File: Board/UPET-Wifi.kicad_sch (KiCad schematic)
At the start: 11 parts, among them U1 ESP32-C3-WROOM-02, U2 SC16IS752IPW, U3 1.8432 MHz

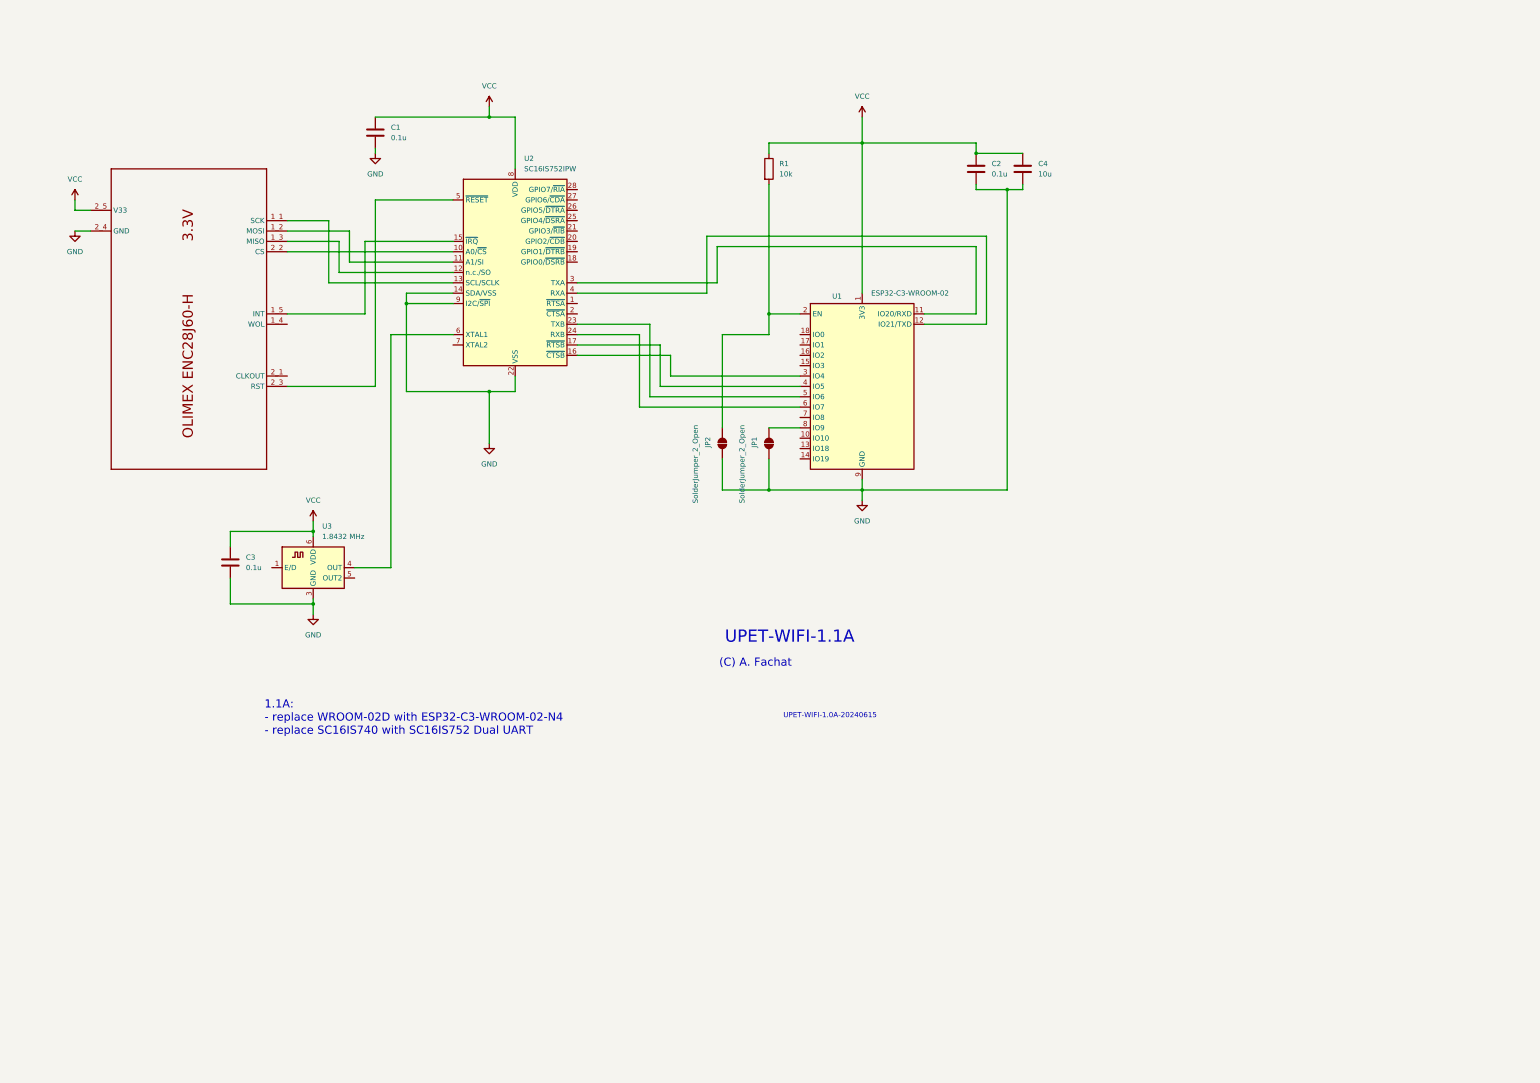
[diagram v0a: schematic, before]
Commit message: move to 1.2 - separate serial prog interface
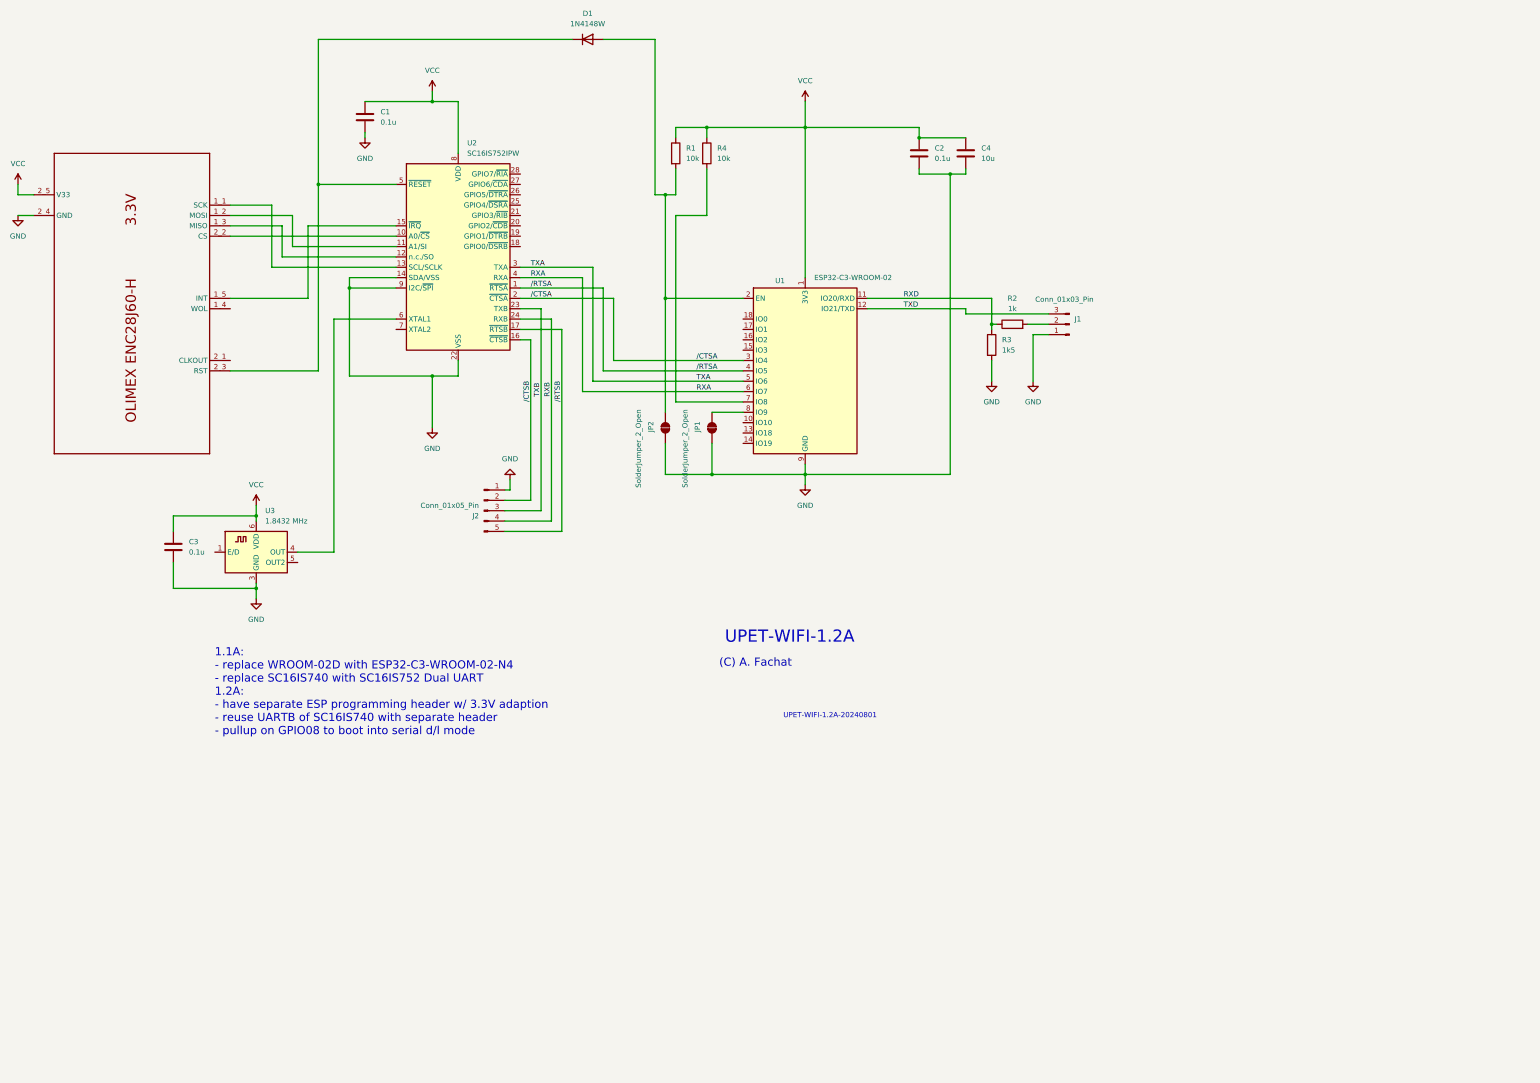
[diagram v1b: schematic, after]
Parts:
- added D1: 1N4148W, Diode_SMD:D_SOD-123, symbol Diode:1N4148W
- added J1: Conn_01x03_Pin, Connector_PinHeader_2.54mm:PinHeader_1x03_P2.54mm_Vertical, symbol Connector:Conn_01x03_Pin
- added J2: Conn_01x05_Pin, Connector_PinHeader_2.54mm:PinHeader_1x05_P2.54mm_Vertical, symbol Connector:Conn_01x05_Pin
- added R2: 1k, Resistor_SMD:R_0603_1608Metric_Pad0.98x0.95mm_HandSolder, symbol Device:R
- added R3: 1k5, Resistor_SMD:R_0603_1608Metric_Pad0.98x0.95mm_HandSolder, symbol Device:R
- added R4: 10k, Resistor_SMD:R_0603_1608Metric_Pad0.98x0.95mm_HandSolder, symbol Device:R
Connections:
- net GND: now also J1.1 (Pin_1), J2.1 (Pin_1), R3.2
- net VCC: now also R4.1
- net at U$1.2_3 (RST), U2.5 (~{RESET}): now also D1.1 (K)
- net at JP2.2 (B), R1.2, U1.2 (EN): now also D1.2 (A)
- net RXD: now reaches U1.11 (IO20/RXD)
- net RXD: now also R2.1, R3.1; no longer U2.3 (TXA)
- net RXA: now reaches U2.4 (RXA)
- net RXA: now also U1.6 (IO7); no longer U1.12 (IO21/TXD)
- net /CTSA: now reaches U1.3 (IO4)
- net /CTSA: now also U2.2 (~{CTSA}); no longer U2.16 (~{CTSB})
- net /RTSA: now reaches U1.4 (IO5)
- net /RTSA: now also U2.1 (~{RTSA}); no longer U2.17 (~{RTSB})
- net TXA: now reaches U1.5 (IO6)
- net TXA: now also U2.3 (TXA); no longer U2.23 (TXB)
- net RXB: now reaches U2.24 (RXB)
- net RXB: now also J2.4 (Pin_4); no longer U1.6 (IO7)
- net at U1.7 (IO8): now also R4.2
- new net: J1.2 (Pin_2), R2.2
- new net TXB: J2.3 (Pin_3), U2.23 (TXB)
- new net TXD: J1.3 (Pin_3), U1.12 (IO21/TXD)
- new net /CTSB: J2.2 (Pin_2), U2.16 (~{CTSB})
- new net /RTSB: J2.5 (Pin_5), U2.17 (~{RTSB})
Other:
- note added: "1.1A: - replace WROOM-02D with ESP32-C3-WROOM-02-N4 - replace SC16IS740 with SC16IS752 Dual UART 1.2A: - have separate ESP programming header w/ 3.3V adaption - reuse UARTB of SC16IS740 with separate header - pullup on GPIO08 to boot into serial d/l mode"
- note added: "UPET-WIFI-1.2A"
- note added: "UPET-WIFI-1.2A-20240801"
- note removed: "1.1A: - replace WROOM-02D with ESP32-C3-WROOM-02-N4 - replace SC16IS740 with SC16IS752 Dual UART"
- note removed: "UPET-WIFI-1.0A-20240615"
- note removed: "UPET-WIFI-1.1A"
- moved on the sheet: C1, C2, C3, C4, JP1, JP2, R1, U1, U2, U3

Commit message: work on wifi 1.3a
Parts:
- removed J1: Conn_01x03_Pin, Connector_PinHeader_2.54mm:PinHeader_1x03_P2.54mm_Vertical, symbol Connector:Conn_01x03_Pin
- removed J2: Conn_01x05_Pin, Connector_PinHeader_2.54mm:PinHeader_1x05_P2.54mm_Vertical, symbol Connector:Conn_01x05_Pin
- added J1: Conn_01x06, Connector_PinHeader_2.54mm:PinHeader_1x06_P2.54mm_Vertical, symbol Connector_Generic:Conn_01x06
- added J3: Conn_01x09, Connector_PinHeader_2.54mm:PinHeader_1x09_P2.54mm_Vertical, symbol Connector_Generic:Conn_01x09
- added Q1, Q2: S8050, Package_TO_SOT_SMD:SOT-23, symbol Transistor_BJT:S8050
- added R5, R6: 12k, Resistor_SMD:R_0603_1608Metric_Pad0.98x0.95mm_HandSolder, symbol Device:R
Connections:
- net GND: now also J1.1 (Pin_1), J3.1 (Pin_1)
- net RXB: now also J3.4 (Pin_4)
- net TXB: now also J3.3 (Pin_3)
- net TXD: now also J1.4 (Pin_4)
- net /CTSB: now also J3.2 (Pin_2)
- net /RTSB: now also J3.5 (Pin_5)
- net at D1.2 (A), JP2.2 (B), R1.2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: now also Q1.3 (C)
- net at JP1.2 (B), U1.8 (IO9): now also Q2.3 (C)
- net at R2.2: now also J1.3 (Pin_3)
- net /DSRB: now reaches U2.18 (GPIO0/~{DSRB})
- net /DSRB: now also J3.6 (Pin_6)
- net /DTRB: now reaches U2.19 (GPIO1/~{DTRB})
- net /DTRB: now also J3.7 (Pin_7)
- net /CDB: now reaches U2.20 (GPIO2/~{CDB})
- net /CDB: now also J3.8 (Pin_8)
- net /RIB: now reaches U2.21 (GPIO3/~{RIB})
- net /RIB: now also J3.9 (Pin_9)
- new net: Q2.1 (B), R5.1
- new net: J1.6 (Pin_6), Q2.2 (E), R6.2
- new net: J1.2 (Pin_2), Q1.2 (E), R5.2
- new net: Q1.1 (B), R6.1
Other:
- moved on the sheet: R2, R3

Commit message: production files
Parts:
- added JP3: SolderJumper_2_Open, Jumper:SolderJumper-2_P1.3mm_Open_RoundedPad1.0x1.5mm, symbol Jumper:SolderJumper_2_Open
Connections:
- net RXD: now also JP3.2 (B)
- net at J1.3 (Pin_3), R2.2: now also JP3.1 (A)
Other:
- note added: "1.1A: - replace WROOM-02D with ESP32-C3-WROOM-02-N4 - replace SC16IS740 with SC16IS752 Dual UART 1.2A: - have separate ESP programming header w/ 3.3V adaption - reuse UARTB of SC16IS740 with separate header - pullup on GPIO08 to boot into serial d/l mode 1.3A: - wider serial connectors - allow use of /RTS and /DTR for ESP control - Programming serial option 3.3V/5V via JP3"
- note added: "Short JP3 if Programming with 3.3V"
- note added: "UPET-WIFI-1.3A"
- note added: "UPET-WIFI-1.3A-20250122"
- note removed: "1.1A: - replace WROOM-02D with ESP32-C3-WROOM-02-N4 - replace SC16IS740 with SC16IS752 Dual UART 1.2A: - have separate ESP programming header w/ 3.3V adaption - reuse UARTB of SC16IS740 with separate header - pullup on GPIO08 to boot into serial d/l mode"
- note removed: "UPET-WIFI-1.2A"
- note removed: "UPET-WIFI-1.2A-20240801"
- moved on the sheet: C3, U3
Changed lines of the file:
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@@
 	(paper "A4")
 	(junction
-		(at 76.2 158.75)
+		(at 86.36 148.59)
 		(diameter 0)
 		(color 0 0 0 0)
@@
 	)
 	(junction
+		(at 255.27 87.63)
+		(diameter 0)
+		(color 0 0 0 0)
+	)
+	(junction
 		(at 190.5 115.57)
 		(diameter 0)
@@
 	)
 	(junction
-		(at 76.2 140.97)
+		(at 86.36 130.81)
 		(diameter 0)
 		(color 0 0 0 0)
@@
 	(wire
 		(pts
-			(xy 86.36 149.86) (xy 95.25 149.86)
+			(xy 96.52 139.7) (xy 105.41 139.7)
 		)
 		(stroke
@@
 	(wire
 		(pts
+			(xy 255.27 77.47) (xy 255.27 87.63)
+		)
+		(stroke
+			(width 0)
+			(type default)
+		)
+	)
+	(wire
+		(pts
 			(xy 210.82 130.81) (xy 187.96 130.81)
 		)
@@
 	(wire
 		(pts
-			(xy 76.2 138.43) (xy 76.2 140.97)
+			(xy 86.36 128.27) (xy 86.36 130.81)
 		)
 		(stroke
@@
 	(wire
 		(pts
+			(xy 255.27 87.63) (xy 271.78 87.63)
+		)
+		(stroke
+			(width 0)
+			(type default)
+		)
+	)
+	(wire
+		(pts
 			(xy 140.97 87.63) (xy 172.72 87.63)
 		)
@@
 	(wire
 		(pts
-			(xy 76.2 140.97) (xy 55.88 140.97)
+			(xy 86.36 130.81) (xy 66.04 130.81)
 		)
 		(stroke
@@
 	(wire
 		(pts
-			(xy 55.88 140.97) (xy 55.88 144.78)
+			(xy 66.04 130.81) (xy 66.04 134.62)
 		)
 		(stroke
@@
 	(wire
 		(pts
+			(xy 242.57 77.47) (xy 241.3 77.47)
+		)
+		(stroke
+			(width 0)
+			(type default)
+		)
+	)
+	(wire
+		(pts
 			(xy 88.9 69.85) (xy 88.9 87.63)
 		)
@@
 	(wire
 		(pts
-			(xy 76.2 157.48) (xy 76.2 158.75)
+			(xy 86.36 147.32) (xy 86.36 148.59)
 		)
 		(stroke
@@
 	(wire
 		(pts
-			(xy 55.88 158.75) (xy 55.88 152.4)
+			(xy 66.04 148.59) (xy 66.04 142.24)
 		)
 		(stroke
@@
 	(wire
 		(pts
-			(xy 95.25 92.71) (xy 110.49 92.71)
+			(xy 105.41 92.71) (xy 110.49 92.71)
 		)
 		(stroke
@@
 	(wire
 		(pts
-			(xy 76.2 158.75) (xy 76.2 161.29)
+			(xy 86.36 148.59) (xy 86.36 151.13)
 		)
 		(stroke
@@
 	(wire
 		(pts
-			(xy 76.2 140.97) (xy 76.2 142.24)
+			(xy 250.19 77.47) (xy 255.27 77.47)
+		)
+		(stroke
+			(width 0)
+			(type default)
+		)
+	)
+	(wire
+		(pts
+			(xy 86.36 130.81) (xy 86.36 132.08)
 		)
 		(stroke
@@
 	(wire
 		(pts
+			(xy 241.3 77.47) (xy 241.3 87.63)
+		)
+		(stroke
+			(width 0)
+			(type default)
+		)
+	)
+	(wire
+		(pts
 			(xy 238.76 48.26) (xy 238.76 45.72)
 		)
@@
 	(wire
 		(pts
-			(xy 95.25 149.86) (xy 95.25 92.71)
+			(xy 105.41 139.7) (xy 105.41 92.71)
 		)
 		(stroke
@@
 	(wire
 		(pts
-			(xy 250.19 87.63) (xy 271.78 87.63)
+			(xy 250.19 87.63) (xy 255.27 87.63)
 		)
 		(stroke
@@
 	(wire
 		(pts
-			(xy 76.2 158.75) (xy 55.88 158.75)
+			(xy 86.36 148.59) (xy 66.04 148.59)
 		)
 		(stroke
@@
 		)
 	)
-	(text "1.1A:\n- replace WROOM-02D with ESP32-C3-WROOM-02-N4\n- replace SC16IS740 with SC16IS752 Dual UART\n1.2A:\n- have separate ESP programming header w/ 3.3V adaption\n- reuse UARTB of SC16IS740 with separate header\n- pullup on GPIO08 to boot into serial d/l mode"
+	(text "1.1A:\n- replace WROOM-02D with ESP32-C3-WROOM-02-N4\n- replace SC16IS740 with SC16IS752 Dual UART\n1.2A:\n- have separate ESP programming header w/ 3.3V adaption\n- reuse UARTB of SC16IS740 with separate header\n- pullup on GPIO08 to boot into serial d/l mode\n1.3A:\n- wider serial connectors\n- allow use of /RTS and /DTR for ESP control\n- Programming serial option 3.3V/5V via JP3"
 		(exclude_from_sim no)
-		(at 66.04 184.15 0)
+		(at 38.862 177.8 0)
 		(effects
 			(font
@@
 		)
 	)
-	(text "UPET-WIFI-1.2A\n"
+	(text "Short JP3 if\nProgramming\nwith 3.3V"
+		(exclude_from_sim no)
+		(at 253.492 73.152 0)
+		(effects
+			(font
+				(size 1.27 1.27)
+			)
+		)
+	)
+	(text "UPET-WIFI-1.3A\n"
 		(exclude_from_sim no)
 		(at 207.01 170.688 0)
@@
 		)
 	)
-	(text "UPET-WIFI-1.2A-20240801\n"
+	(text "UPET-WIFI-1.3A-20250122"
 		(exclude_from_sim no)
 		(at 216.916 189.992 0)
@@
 	(symbol
 		(lib_id "Oscillator:XUX71")
-		(at 76.2 149.86 0)
+		(at 86.36 139.7 0)
 		(unit 1)
 		(exclude_from_sim no)
@@
 		(fields_autoplaced yes)
 		(property "Reference" "U3"
-			(at 78.3941 139.7 0)
+			(at 88.5541 129.54 0)
 			(effects
 				(font
@@
 		)
 		(property "Value" "1.8432 MHz"
-			(at 78.3941 142.24 0)
+			(at 88.5541 132.08 0)
 			(effects
 				(font
@@
 		)
 		(property "Footprint" "Oscillator:Oscillator_SMD_IDT_JU6-6_7.0x5.0mm_P2.54mm"
-			(at 77.47 158.75 0)
+			(at 87.63 148.59 0)
 			(effects
 				(font
@@
 		)
 		(property "Datasheet" "https://www.renesas.com/us/en/document/dst/xu-family-low-phase-noise-quartz-based-pll-oscillators-datasheet"
-			(at 66.04 132.08 0)
+			(at 76.2 121.92 0)
 			(effects
 				(font
@@
 		)
 		(property "Description" "Low phase noise, quartz-based PLL oscillator, 0.016-1500 MHz, complementary output"
-			(at 76.2 149.86 0)
+			(at 86.36 139.7 0)
 			(effects
 				(font
@@
 	(symbol
 		(lib_id "power:GND")
-		(at 76.2 161.29 0)
+		(at 86.36 151.13 0)
 		(unit 1)
 		(exclude_from_sim no)
@@
 		(fields_autoplaced yes)
 		(property "Reference" "#PWR08"
-			(at 76.2 167.64 0)
+			(at 86.36 157.48 0)
 			(effects
 				(font
@@
 		)
 		(property "Value" "GND"
-			(at 76.2 166.37 0)
+			(at 86.36 156.21 0)
 			(effects
 				(font
@@
 		)
 		(property "Footprint" ""
-			(at 76.2 161.29 0)
+			(at 86.36 151.13 0)
 			(effects
 				(font
@@
 		)
 		(property "Datasheet" ""
-			(at 76.2 161.29 0)
+			(at 86.36 151.13 0)
 			(effects
 				(font
@@
 		)
 		(property "Description" "Power symbol creates a global label with name \"GND\" , ground"
-			(at 76.2 161.29 0)
+			(at 86.36 151.13 0)
 			(effects
 				(font
@@
 	)
 	(symbol
+		(lib_id "Jumper:SolderJumper_2_Open")
+		(at 246.38 77.47 180)
+		(unit 1)
+		(exclude_from_sim yes)
+		(in_bom no)
+		(on_board yes)
+		(dnp no)
+		(property "Reference" "JP3"
+			(at 246.126 81.026 0)
+			(effects
+				(font
+					(size 1.27 1.27)
+				)
+			)
+		)
+		(property "Value" "SolderJumper_2_Open"
+			(at 275.336 67.056 0)
+			(effects
+				(font
+					(size 1.27 1.27)
+				)
+				(hide yes)
+			)
+		)
+		(property "Footprint" "Jumper:SolderJumper-2_P1.3mm_Open_RoundedPad1.0x1.5mm"
+			(at 246.38 77.47 0)
+			(effects
+				(font
+					(size 1.27 1.27)
+				)
+				(hide yes)
+			)
+		)
+		(property "Datasheet" "~"
+			(at 246.38 77.47 0)
+			(effects
+				(font
+					(size 1.27 1.27)
+				)
+				(hide yes)
+			)
+		)
+		(property "Description" "Solder Jumper, 2-pole, open"
+			(at 246.38 77.47 0)
+			(effects
+				(font
+					(size 1.27 1.27)
+				)
+				(hide yes)
+			)
+		)
+		(pin "1"
+		)
+		(pin "2"
+		)
+		(instances
+			(project "UPET-Wifi"
+				(path "/f84449d7-983f-4b4b-88bd-503f175f0b89"
+					(reference "JP3")
+					(unit 1)
+				)
+			)
+		)
+	)
+	(symbol
 		(lib_id "Device:C")
 		(at 102.87 43.18 0)
@@
 		(on_board yes)
 		(dnp no)
-		(fields_autoplaced yes)
 		(property "Reference" "R2"
-			(at 246.38 81.28 90)
+			(at 244.856 84.328 90)
 			(effects
 				(font
@@
 		)
 		(property "Value" "1k"
-			(at 246.38 83.82 90)
+			(at 248.666 84.328 90)
 			(effects
 				(font
@@
 	(symbol
 		(lib_id "Device:C")
-		(at 55.88 148.59 0)
+		(at 66.04 138.43 0)
 		(unit 1)
 		(exclude_from_sim no)
@@
 		(fields_autoplaced yes)
 		(property "Reference" "C3"
-			(at 59.69 147.3199 0)
+			(at 69.85 137.1599 0)
 			(effects
 				(font
@@
 		)
 		(property "Value" "0.1u"
-			(at 59.69 149.8599 0)
+			(at 69.85 139.6999 0)
 			(effects
 				(font
@@
 		)
 		(property "Footprint" "Capacitor_SMD:C_0603_1608Metric_Pad1.08x0.95mm_HandSolder"
-			(at 56.8452 152.4 0)
+			(at 67.0052 142.24 0)
 			(effects
 				(font
@@
 		)
 		(property "Datasheet" "~"
-			(at 55.88 148.59 0)
+			(at 66.04 138.43 0)
 			(effects
 				(font
@@
 		)
 		(property "Description" "Unpolarized capacitor"
-			(at 55.88 148.59 0)
+			(at 66.04 138.43 0)
 			(effects
 				(font
@@
 	(symbol
 		(lib_id "power:VCC")
-		(at 76.2 138.43 0)
+		(at 86.36 128.27 0)
 		(unit 1)
 		(exclude_from_sim no)
@@
 		(fields_autoplaced yes)
 		(property "Reference" "#PWR07"
-			(at 76.2 142.24 0)
+			(at 86.36 132.08 0)
 			(effects
 				(font
@@
 		)
 		(property "Value" "VCC"
-			(at 76.2 133.35 0)
+			(at 86.36 123.19 0)
 			(effects
 				(font
@@
 		)
 		(property "Footprint" ""
-			(at 76.2 138.43 0)
+			(at 86.36 128.27 0)
 			(effects
 				(font
@@
 		)
 		(property "Datasheet" ""
-			(at 76.2 138.43 0)
+			(at 86.36 128.27 0)
 			(effects
 				(font
@@
 		)
 		(property "Description" "Power symbol creates a global label with name \"VCC\""
-			(at 76.2 138.43 0)
+			(at 86.36 128.27 0)
 			(effects
 				(font
